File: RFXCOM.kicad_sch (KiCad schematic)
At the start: 9 parts, among them J1 Conn_Coaxial, J2 Conn_Coaxial, J3 Conn_01x01, J4 Rx, J5 Tx, U1 arduino_mega_pro_embedded

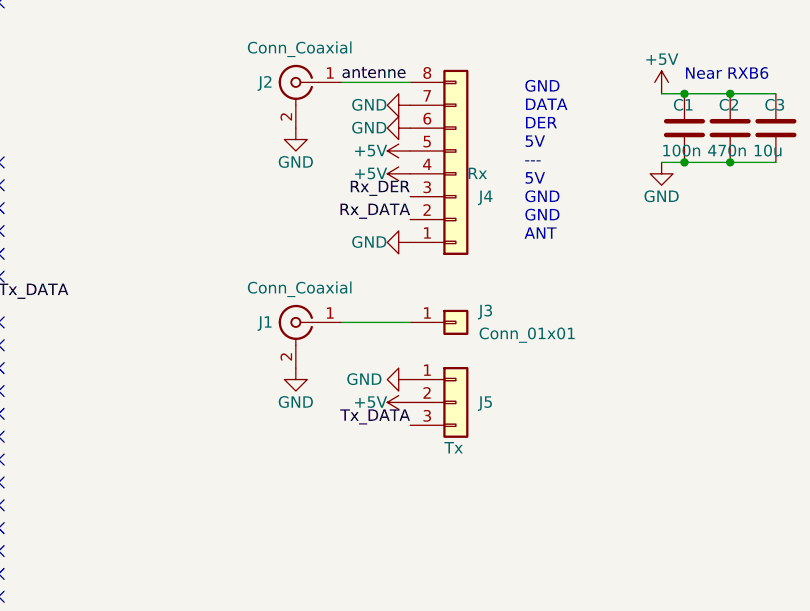
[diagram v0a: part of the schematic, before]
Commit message: Use correct footprint for TX
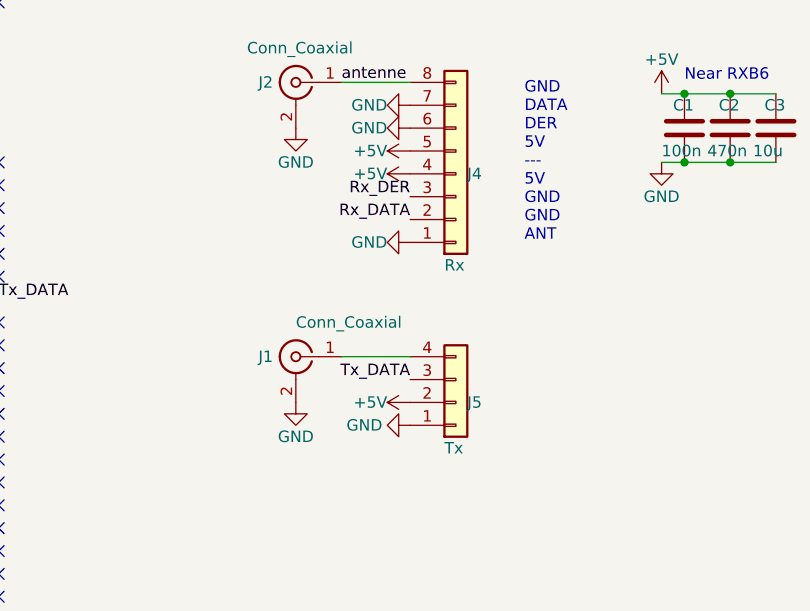
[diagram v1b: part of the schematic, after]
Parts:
- removed J3: Conn_01x01, Connector_PinHeader_2.54mm:PinHeader_1x01_P2.54mm_Vertical, symbol Connector_Generic:Conn_01x01
- J5: footprint Connector_PinHeader_2.54mm:PinHeader_1x03_P2.54mm_Vertical -> rf_components:XKFST_Vertical; symbol Connector_Generic:Conn_01x03 -> Connector_Generic:Conn_01x04
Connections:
- net at J1.1 (In): now also J5.4 (Pin_4)
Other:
- moved on the sheet: J1
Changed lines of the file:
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@@
     (stroke (width 0) (type default) (color 0 0 0 0))
   )
-  (wire (pts (xy 109.22 63.5) (xy 101.6 63.5))
+  (wire (pts (xy 109.22 67.31) (xy 101.6 67.31))
     (stroke (width 0) (type default) (color 0 0 0 0))
   )
@@
     (effects (font (size 1.27 1.27)) (justify left bottom))
   )
-  (label "Tx_DATA" (at 109.22 74.93 180)
+  (label "Tx_DATA" (at 109.22 69.85 180)
     (effects (font (size 1.27 1.27)) (justify right bottom))
   )
@@
   (symbol (lib_id "Connector_Generic:Conn_01x08") (at 114.3 46.99 0) (mirror x) (unit 1)
     (in_bom yes) (on_board yes)
-    (property "Reference" "J4" (id 0) (at 116.84 49.53 0)
-      (effects (font (size 1.27 1.27)) (justify left))
-    )
-    (property "Value" "Rx" (id 1) (at 115.57 46.99 0)
+    (property "Reference" "J4" (id 0) (at 115.57 46.99 0)
+      (effects (font (size 1.27 1.27)) (justify left))
+    )
+    (property "Value" "Rx" (id 1) (at 113.03 57.15 0)
       (effects (font (size 1.27 1.27)) (justify left))
     )
@@
     (pin "1")
   )
-  (symbol (lib_id "Connector_Generic:Conn_01x03") (at 114.3 72.39 0) (unit 1)
-    (in_bom yes) (on_board yes)
-    (property "Reference" "J5" (id 0) (at 116.84 72.39 0)
+  (symbol (lib_id "Connector_Generic:Conn_01x04") (at 114.3 72.39 0) (mirror x) (unit 1)
+    (in_bom yes) (on_board yes)
+    (property "Reference" "J5" (id 0) (at 115.57 72.39 0)
       (effects (font (size 1.27 1.27)) (justify left))
     )
@@
       (effects (font (size 1.27 1.27)) (justify left))
     )
-    (property "Footprint" "Connector_PinHeader_2.54mm:PinHeader_1x03_P2.54mm_Vertical" (id 2) (at 114.3 72.39 0)
+    (property "Footprint" "rf_components:XKFST_Vertical" (id 2) (at 114.3 72.39 0)
       (effects (font (size 1.27 1.27)) hide)
     )
@@
     (pin "2")
     (pin "3")
+    (pin "4")
   )
   (symbol (lib_id "power:+5V") (at 109.22 44.45 90) (unit 1)
@@
     (pin "2")
   )
-  (symbol (lib_id "Connector_Generic:Conn_01x01") (at 114.3 63.5 0) (unit 1)
-    (in_bom yes) (on_board yes) (fields_autoplaced)
-    (property "Reference" "J3" (id 0) (at 116.84 62.2299 0)
-      (effects (font (size 1.27 1.27)) (justify left))
-    )
-    (property "Value" "Conn_01x01" (id 1) (at 116.84 64.7699 0)
-      (effects (font (size 1.27 1.27)) (justify left))
-    )
-    (property "Footprint" "Connector_PinHeader_2.54mm:PinHeader_1x01_P2.54mm_Vertical" (id 2) (at 114.3 63.5 0)
-      (effects (font (size 1.27 1.27)) hide)
-    )
-    (property "Datasheet" "~" (id 3) (at 114.3 63.5 0)
-      (effects (font (size 1.27 1.27)) hide)
-    )
-    (pin "1")
-  )
-  (symbol (lib_id "power:GND") (at 109.22 69.85 270) (unit 1)
-    (in_bom yes) (on_board yes)
-    (property "Reference" "#PWR010" (id 0) (at 102.87 69.85 0)
-      (effects (font (size 1.27 1.27)) hide)
-    )
-    (property "Value" "GND" (id 1) (at 104.14 69.85 90))
-    (property "Footprint" "" (id 2) (at 109.22 69.85 0)
-      (effects (font (size 1.27 1.27)) hide)
-    )
-    (property "Datasheet" "" (id 3) (at 109.22 69.85 0)
+  (symbol (lib_id "power:GND") (at 109.22 74.93 270) (mirror x) (unit 1)
+    (in_bom yes) (on_board yes)
+    (property "Reference" "#PWR010" (id 0) (at 102.87 74.93 0)
+      (effects (font (size 1.27 1.27)) hide)
+    )
+    (property "Value" "GND" (id 1) (at 104.14 74.93 90))
+    (property "Footprint" "" (id 2) (at 109.22 74.93 0)
+      (effects (font (size 1.27 1.27)) hide)
+    )
+    (property "Datasheet" "" (id 3) (at 109.22 74.93 0)
       (effects (font (size 1.27 1.27)) hide)
     )
@@
     (pin "1")
   )
-  (symbol (lib_id "Connector:Conn_Coaxial") (at 96.52 63.5 0) (mirror y) (unit 1)
-    (in_bom yes) (on_board yes)
-    (property "Reference" "J1" (id 0) (at 93.98 63.5 0)
-      (effects (font (size 1.27 1.27)) (justify left))
-    )
-    (property "Value" "Conn_Coaxial" (id 1) (at 102.87 59.69 0)
-      (effects (font (size 1.27 1.27)) (justify left))
-    )
-    (property "Footprint" "Connector_Coaxial:SMA_Amphenol_901-144_Vertical" (id 2) (at 96.52 63.5 0)
-      (effects (font (size 1.27 1.27)) hide)
-    )
-    (property "Datasheet" " ~" (id 3) (at 96.52 63.5 0)
+  (symbol (lib_id "Connector:Conn_Coaxial") (at 96.52 67.31 0) (mirror y) (unit 1)
+    (in_bom yes) (on_board yes)
+    (property "Reference" "J1" (id 0) (at 93.98 67.31 0)
+      (effects (font (size 1.27 1.27)) (justify left))
+    )
+    (property "Value" "Conn_Coaxial" (id 1) (at 96.52 63.5 0)
+      (effects (font (size 1.27 1.27)) (justify right))
+    )
+    (property "Footprint" "Connector_Coaxial:SMA_Amphenol_901-144_Vertical" (id 2) (at 96.52 67.31 0)
+      (effects (font (size 1.27 1.27)) hide)
+    )
+    (property "Datasheet" " ~" (id 3) (at 96.52 67.31 0)
       (effects (font (size 1.27 1.27)) hide)
     )
@@
     (pin "VIN_2")
   )
-  (symbol (lib_id "power:+5V") (at 109.22 72.39 90) (unit 1)
+  (symbol (lib_id "power:+5V") (at 109.22 72.39 90) (mirror x) (unit 1)
     (in_bom yes) (on_board yes)
     (property "Reference" "#PWR011" (id 0) (at 113.03 72.39 0)
@@
     (pin "1")
   )
-  (symbol (lib_id "power:GND") (at 96.52 68.58 0) (unit 1)
-    (in_bom yes) (on_board yes)
-    (property "Reference" "#PWR01" (id 0) (at 96.52 74.93 0)
-      (effects (font (size 1.27 1.27)) hide)
-    )
-    (property "Value" "GND" (id 1) (at 96.52 72.39 0))
-    (property "Footprint" "" (id 2) (at 96.52 68.58 0)
-      (effects (font (size 1.27 1.27)) hide)
-    )
-    (property "Datasheet" "" (id 3) (at 96.52 68.58 0)
+  (symbol (lib_id "power:GND") (at 96.52 72.39 0) (unit 1)
+    (in_bom yes) (on_board yes)
+    (property "Reference" "#PWR01" (id 0) (at 96.52 78.74 0)
+      (effects (font (size 1.27 1.27)) hide)
+    )
+    (property "Value" "GND" (id 1) (at 96.52 76.2 0))
+    (property "Footprint" "" (id 2) (at 96.52 72.39 0)
+      (effects (font (size 1.27 1.27)) hide)
+    )
+    (property "Datasheet" "" (id 3) (at 96.52 72.39 0)
       (effects (font (size 1.27 1.27)) hide)
     )
@@
       (reference "J2") (unit 1) (value "Conn_Coaxial") (footprint "Connector_Coaxial:SMA_Amphenol_901-144_Vertical")
     )
-    (path "/6d730227-a281-4ca9-8dba-d01c6728708d"
-      (reference "J3") (unit 1) (value "Conn_01x01") (footprint "Connector_PinHeader_2.54mm:PinHeader_1x01_P2.54mm_Vertical")
-    )
     (path "/322da0ba-a86d-429d-ab15-bb0db3104e36"
       (reference "J4") (unit 1) (value "Rx") (footprint "rf_components:RXB6")
     )
     (path "/4a3136df-385b-416b-a9b3-d730d73e2ec4"
-      (reference "J5") (unit 1) (value "Tx") (footprint "Connector_PinHeader_2.54mm:PinHeader_1x03_P2.54mm_Vertical")
+      (reference "J5") (unit 1) (value "Tx") (footprint "rf_components:XKFST_Vertical")
     )
     (path "/cd27ac41-7750-4b04-b00e-ebd166bb4e58"
